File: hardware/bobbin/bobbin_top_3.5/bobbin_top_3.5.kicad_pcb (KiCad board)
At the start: 2 copper layers, 78.5 x 8.5 mm, 1 part

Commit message: new scheme
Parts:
- H3: footprint cycfi_library:single-pad-10x2 -> cycfi_library:xr2-3.5-bobbin-top
- moved H3 2.60 mm to (134.0, 65.0)
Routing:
- net GND: track 0.00 -> 2.70 mm, vias 2 -> 1
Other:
- outline, holes or cut-outs redrawn
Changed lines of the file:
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@@
   (general
     (thickness 1.6)
-    (drawings 20)
+    (drawings 12)
     (tracks 2)
     (zones 0)
@@
     (44 Edge.Cuts user)
     (45 Margin user)
-    (46 B.CrtYd user hide)
-    (47 F.CrtYd user hide)
-    (48 B.Fab user hide)
-    (49 F.Fab user hide)
+    (46 B.CrtYd user)
+    (47 F.CrtYd user)
+    (48 B.Fab user)
+    (49 F.Fab user)
   )
   (setup
@@
     (add_net GND)
   )
-  (module cycfi_library:single-pad-10x2 (layer F.Cu)
-    (at 134 62.4)
-    (fp_text reference H3 (at 6.5 0.1) (layer F.SilkS) hide
+  (module cycfi_library:xr2-3.5-bobbin-top (layer F.Cu)
+    (at 134 65)
+    (fp_text reference H3 (at 0 6) (layer F.SilkS)
       (effects (font (size 1 1) (thickness 0.15)))
     )
-    (fp_text value single_pad_smd (at 0 -2.54) (layer F.Fab)
+    (fp_text value single_pad_smd (at 0 -4) (layer F.Fab)
       (effects (font (size 1 1) (thickness 0.15)))
     )
-    (pad 1 smd rect (at 0 0) (size 10 2) (layers F.Cu F.Paste F.Mask)
+    (pad 1 thru_hole oval (at 0 0) (size 72.5 2.5) (drill oval 72 2) (layers *.Cu *.Mask)
       (net 1 GND))
   )
-  (gr_line (start 129 61.4) (end 129 63.4) (layer Dwgs.User) (width 0.05))
-  (gr_line (start 129 63.4) (end 139 63.4) (layer Dwgs.User) (width 0.05))
-  (gr_line (start 139 63.4) (end 139 61.4) (layer Dwgs.User) (width 0.05))
-  (gr_line (start 139 61.4) (end 129 61.4) (layer Dwgs.User) (width 0.05))
   (gr_arc (start 169 65) (end 169 69.25) (angle -180) (layer Edge.Cuts) (width 0.05))
-  (gr_line (start 169 64) (end 169 66) (layer Edge.Cuts) (width 0.05))
-  (gr_line (start 99 66) (end 169 66) (layer Edge.Cuts) (width 0.05))
-  (gr_line (start 99 64) (end 99 66) (layer Edge.Cuts) (width 0.05))
-  (gr_line (start 99 64) (end 169 64) (layer Edge.Cuts) (width 0.05))
   (gr_line (start 169 69.25) (end 99 69.25) (layer Edge.Cuts) (width 0.05))
   (gr_line (start 99 60.75) (end 169 60.75) (layer Edge.Cuts) (width 0.05))
@@
   (gr_arc (start 99 65) (end 99 60.75) (angle -180) (layer Dwgs.User) (width 0.05))
   (gr_arc (start 169 65) (end 169 69.25) (angle -180) (layer Dwgs.User) (width 0.05))
-  (via (at 128 62.5) (size 0.8) (drill 0.4) (layers F.Cu B.Cu) (net 1))
-  (via (at 140 62.5) (size 0.8) (drill 0.4) (layers F.Cu B.Cu) (net 1))
+  (via (at 134 62.3) (size 0.8) (drill 0.4) (layers F.Cu B.Cu) (net 1))
+  (segment (start 134 62.3) (end 134 65) (width 0.25) (layer B.Cu) (net 1))
   (zone (net 1) (net_name GND) (layer F.Cu) (hatch edge 0.508)
     (connect_pads yes (clearance 0.25))
@@
     (polygon
       (pts
-        (xy 174 70) (xy 94 70) (xy 94 60) (xy 174 60)
+        (xy 173.3 69.3) (xy 94.7 69.3) (xy 94.7 60.7) (xy 173.3 60.7)
       )
     )
@@
     (polygon
       (pts
-        (xy 174 70) (xy 94 70) (xy 94 60) (xy 174 60)
+        (xy 173.2 69.4) (xy 94.7 69.3) (xy 94.7 60.7) (xy 173.3 60.7)
       )
     )

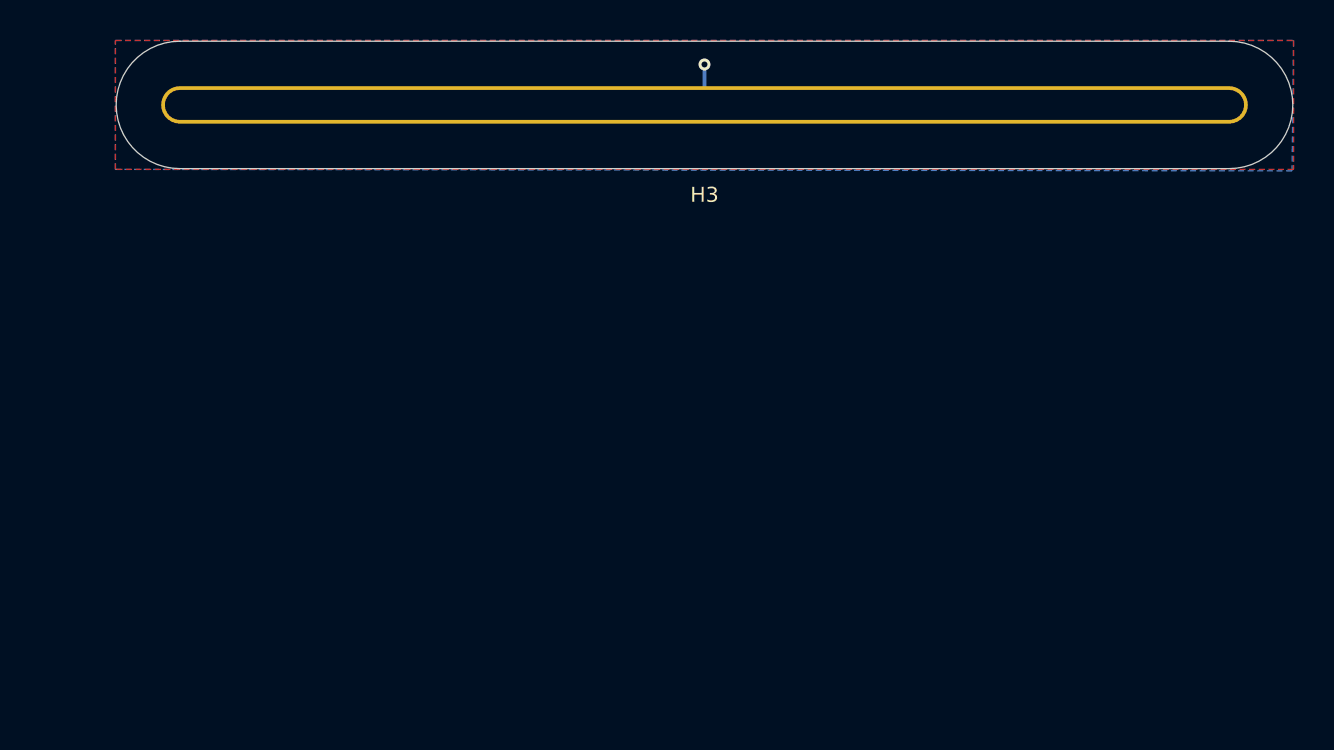
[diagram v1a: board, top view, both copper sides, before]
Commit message: Copied over bobbin_bottom to bobbin_top
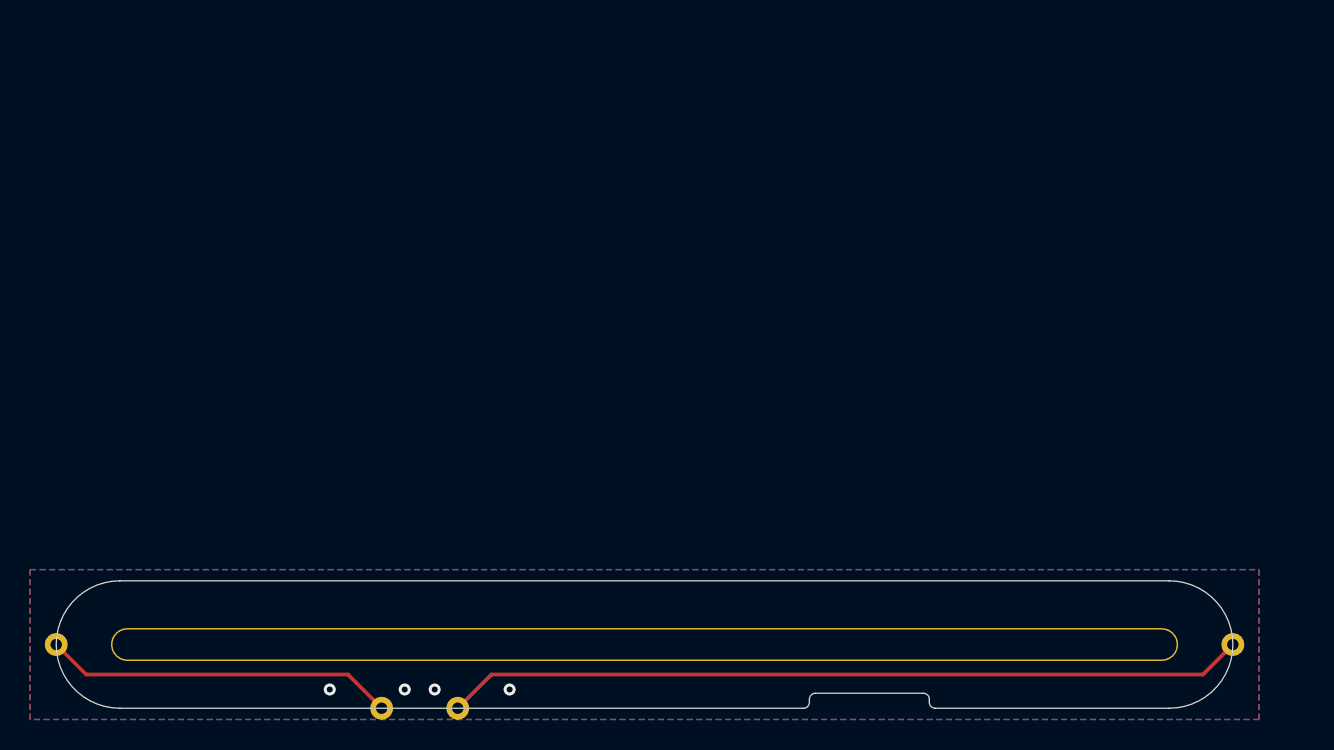
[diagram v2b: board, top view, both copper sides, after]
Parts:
- removed H3: single_pad_smd, cycfi_library:xr2-3.5-bobbin-top
- added H1: single_pad, xr_spectra_library:rail_slot_3.5, F.Cu at (129.8, 101.0)
- added J1: OC, cycfi_library:single-pad-1.52x1.52-th, F.Cu at (117.5, 105.2)
- added J2: OC, cycfi_library:single-pad-1.52x1.52-th, F.Cu at (169.2, 101.0)
- added J3: IC, cycfi_library:single-pad-1.52x1.52-th, F.Cu at (90.8, 101.0)
- added J4: IC, cycfi_library:single-pad-1.52x1.52-th, F.Cu at (112.5, 105.2)
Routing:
- net /OC: track 0.00 -> 53.5 mm
- net /IC: track 0.00 -> 23.5 mm
- net GND: track 2.70 -> 0.00 mm, vias 1 -> 4
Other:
- outline, holes or cut-outs redrawn
- net class Default removed

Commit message: Bobbin-top done
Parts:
- removed J1, J2: OC, cycfi_library:single-pad-1.52x1.52-th
- removed J3, J4: IC, cycfi_library:single-pad-1.52x1.52-th
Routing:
- net /OC: track 53.5 -> 0.00 mm
- net /IC: track 23.5 -> 0.00 mm
- net GND: vias 4 -> 0
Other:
- outline, holes or cut-outs redrawn
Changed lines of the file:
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@@
   (net 0 "")
   (net 1 "GND")
-  (net 2 "/OC")
-  (net 3 "/IC")
-  (footprint "cycfi_library:single-pad-1.52x1.52-th" (layer "F.Cu")
-    (at 117.54 105.25 180)
-    (property "Sheetfile" "bobbin_bottom_3.5.kicad_sch")
-    (property "Sheetname" "")
-    (attr through_hole)
-    (fp_text reference "J1" (at 0 2.54 180) (layer "F.SilkS") hide
-      (effects (font (size 1 1) (thickness 0.15)))
-    )
-    (fp_text value "OC" (at 0 -2.54 180) (layer "F.Fab")
-      (effects (font (size 1 1) (thickness 0.15)))
-    )
-    (pad "1" thru_hole circle (at 0 0 180) (size 1.52 1.52) (drill 0.76) (layers *.Cu *.Mask)
-      (net 2 "/OC") (pinfunction "Pin_1") (pintype "passive"))
-  )
-  (footprint "cycfi_library:single-pad-1.52x1.52-th" (layer "F.Cu")
-    (at 169.25 101 180)
-    (property "Sheetfile" "bobbin_bottom_3.5.kicad_sch")
-    (property "Sheetname" "")
-    (attr through_hole)
-    (fp_text reference "J2" (at 0 2.54) (layer "F.SilkS") hide
-      (effects (font (size 1 1) (thickness 0.15)))
-    )
-    (fp_text value "OC" (at -3 -0.09) (layer "F.Fab")
-      (effects (font (size 1 1) (thickness 0.15)))
-    )
-    (pad "1" thru_hole circle (at 0 0 180) (size 1.52 1.52) (drill 0.76) (layers *.Cu *.Mask)
-      (net 2 "/OC") (pinfunction "Pin_1") (pintype "passive"))
-  )
-  (footprint "cycfi_library:single-pad-1.52x1.52-th" (layer "F.Cu")
-    (at 90.75 101)
-    (property "Sheetfile" "bobbin_bottom_3.5.kicad_sch")
-    (property "Sheetname" "")
-    (attr through_hole)
-    (fp_text reference "J3" (at 0 2.54) (layer "F.SilkS") hide
-      (effects (font (size 1 1) (thickness 0.15)))
-    )
-    (fp_text value "IC" (at -2.75 0.08) (layer "F.Fab")
-      (effects (font (size 1 1) (thickness 0.15)))
-    )
-    (pad "1" thru_hole circle (at 0 0) (size 1.52 1.52) (drill 0.76) (layers *.Cu *.Mask)
-      (net 3 "/IC") (pinfunction "Pin_1") (pintype "passive"))
-  )
   (footprint "xr_spectra_library:rail_slot_3.5" (layer "F.Cu")
     (at 129.75 101)
-    (property "Sheetfile" "bobbin_bottom_3.5.kicad_sch")
+    (property "Sheetfile" "bobbin_top_3.5.kicad_sch")
     (property "Sheetname" "")
     (attr through_hole)
@@
     (pad "1" thru_hole oval (at 0.25 0) (size 71.2 2.2) (drill oval 71 2) (layers *.Cu *.Mask)
       (net 1 "GND") (pinfunction "1") (pintype "input"))
-  )
-  (footprint "cycfi_library:single-pad-1.52x1.52-th" (layer "F.Cu")
-    (at 112.46 105.25)
-    (property "Sheetfile" "bobbin_bottom_3.5.kicad_sch")
-    (property "Sheetname" "")
-    (attr through_hole)
-    (fp_text reference "J4" (at 0 2.54) (layer "F.SilkS") hide
-      (effects (font (size 1 1) (thickness 0.15)))
-    )
-    (fp_text value "IC" (at 0 2.25) (layer "F.Fab")
-      (effects (font (size 1 1) (thickness 0.15)))
-    )
-    (pad "1" thru_hole circle (at 0 0) (size 1.52 1.52) (drill 0.76) (layers *.Cu *.Mask)
-      (net 3 "/IC") (pinfunction "Pin_1") (pintype "passive"))
   )
   (gr_arc (start 165 96.75) (mid 169.25 101) (end 165 105.25) (layer "Dwgs.User") (width 0.01))
@@
   (gr_arc (start 141 104.85) (mid 140.882843 105.132843) (end 140.6 105.25) (layer "Dwgs.User") (width 0.01))
   (gr_arc (start 165 96.75) (mid 169.25 101) (end 165 105.25) (layer "Edge.Cuts") (width 0.01))
-  (gr_arc (start 141 104.85) (mid 140.882843 105.132843) (end 140.6 105.25) (layer "Edge.Cuts") (width 0.01))
-  (gr_line (start 165 105.25) (end 149.4 105.25) (layer "Edge.Cuts") (width 0.01))
   (gr_arc (start 95 105.25) (mid 90.75 101) (end 95 96.75) (layer "Edge.Cuts") (width 0.01))
   (gr_line (start 95 96.75) (end 165 96.75) (layer "Edge.Cuts") (width 0.01))
-  (gr_arc (start 148.6 104.25) (mid 148.882843 104.367157) (end 149 104.65) (layer "Edge.Cuts") (width 0.01))
-  (gr_arc (start 149.4 105.25) (mid 149.117157 105.132843) (end 149 104.85) (layer "Edge.Cuts") (width 0.01))
-  (gr_line (start 149 104.65) (end 149 104.85) (layer "Edge.Cuts") (width 0.01))
-  (gr_line (start 141 104.85) (end 141 104.65) (layer "Edge.Cuts") (width 0.01))
-  (gr_line (start 141.4 104.25) (end 148.6 104.25) (layer "Edge.Cuts") (width 0.01))
-  (gr_arc (start 141 104.65) (mid 141.117157 104.367157) (end 141.4 104.25) (layer "Edge.Cuts") (width 0.01))
-  (gr_line (start 140.6 105.25) (end 95 105.25) (layer "Edge.Cuts") (width 0.01))
-  (via (at 109 104) (size 0.8) (drill 0.4) (layers "F.Cu" "B.Cu") (free) (net 1))
-  (via (at 114 104) (size 0.8) (drill 0.4) (layers "F.Cu" "B.Cu") (free) (net 1))
-  (via (at 116 104) (size 0.8) (drill 0.4) (layers "F.Cu" "B.Cu") (free) (net 1))
-  (via (at 121 104) (size 0.8) (drill 0.4) (layers "F.Cu" "B.Cu") (free) (net 1))
-  (segment (start 117.54 105.25) (end 119.79 103) (width 0.25) (layer "F.Cu") (net 2))
-  (segment (start 119.79 103) (end 167.25 103) (width 0.25) (layer "F.Cu") (net 2))
-  (segment (start 167.25 103) (end 169.25 101) (width 0.25) (layer "F.Cu") (net 2))
-  (segment (start 110.21 103) (end 92.75 103) (width 0.25) (layer "F.Cu") (net 3))
-  (segment (start 112.46 105.25) (end 110.21 103) (width 0.25) (layer "F.Cu") (net 3))
-  (segment (start 92.75 103) (end 90.75 101) (width 0.25) (layer "F.Cu") (net 3))
+  (gr_line (start 165 105.25) (end 95 105.25) (layer "Edge.Cuts") (width 0.01))
   (zone (net 1) (net_name "GND") (layer "F.Cu") (hatch edge 0.508)
     (connect_pads (clearance 0.25))
